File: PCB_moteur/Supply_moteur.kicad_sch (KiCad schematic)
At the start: 63 parts, among them J10 BATT12V, J11 BATT1S, J12 EXT_SW, J9 BATT3S1, Q2 PMOS, Q4 MMBT3904, Q5 IRFR5505TRPBF, SW1 POWER BUTTON, U11 LTC2954ITS8-1, U5 TPS61201DRCR, U8 LM1085-5.0

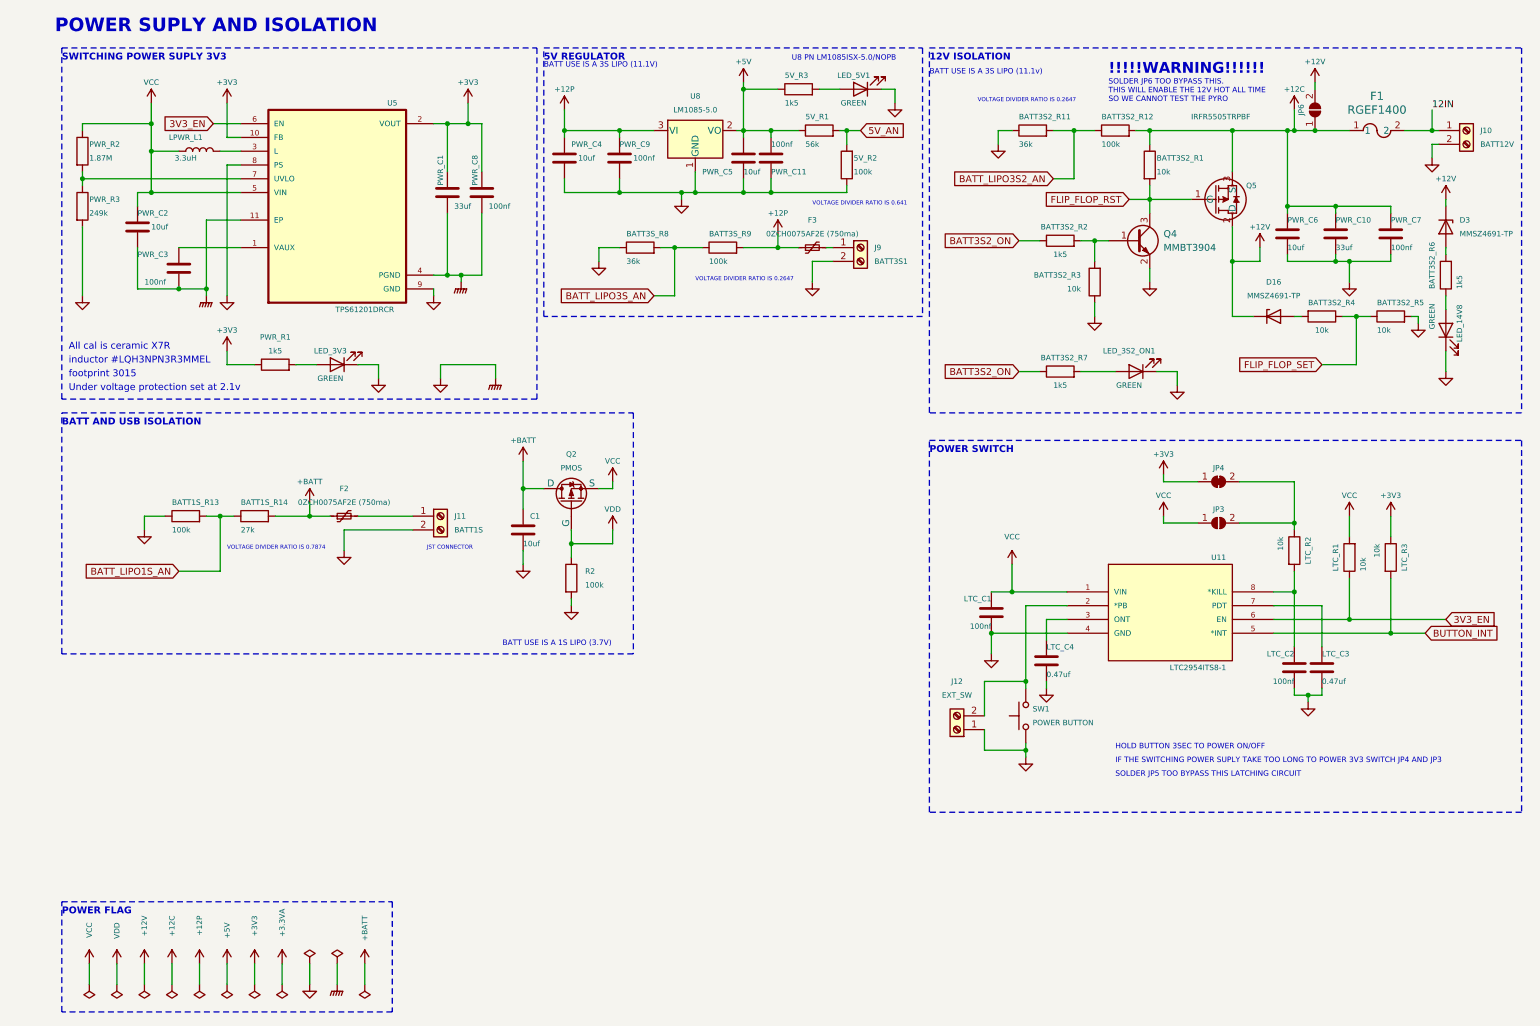
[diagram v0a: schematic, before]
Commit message: Manque supply, pyro et finition (découplage etc)
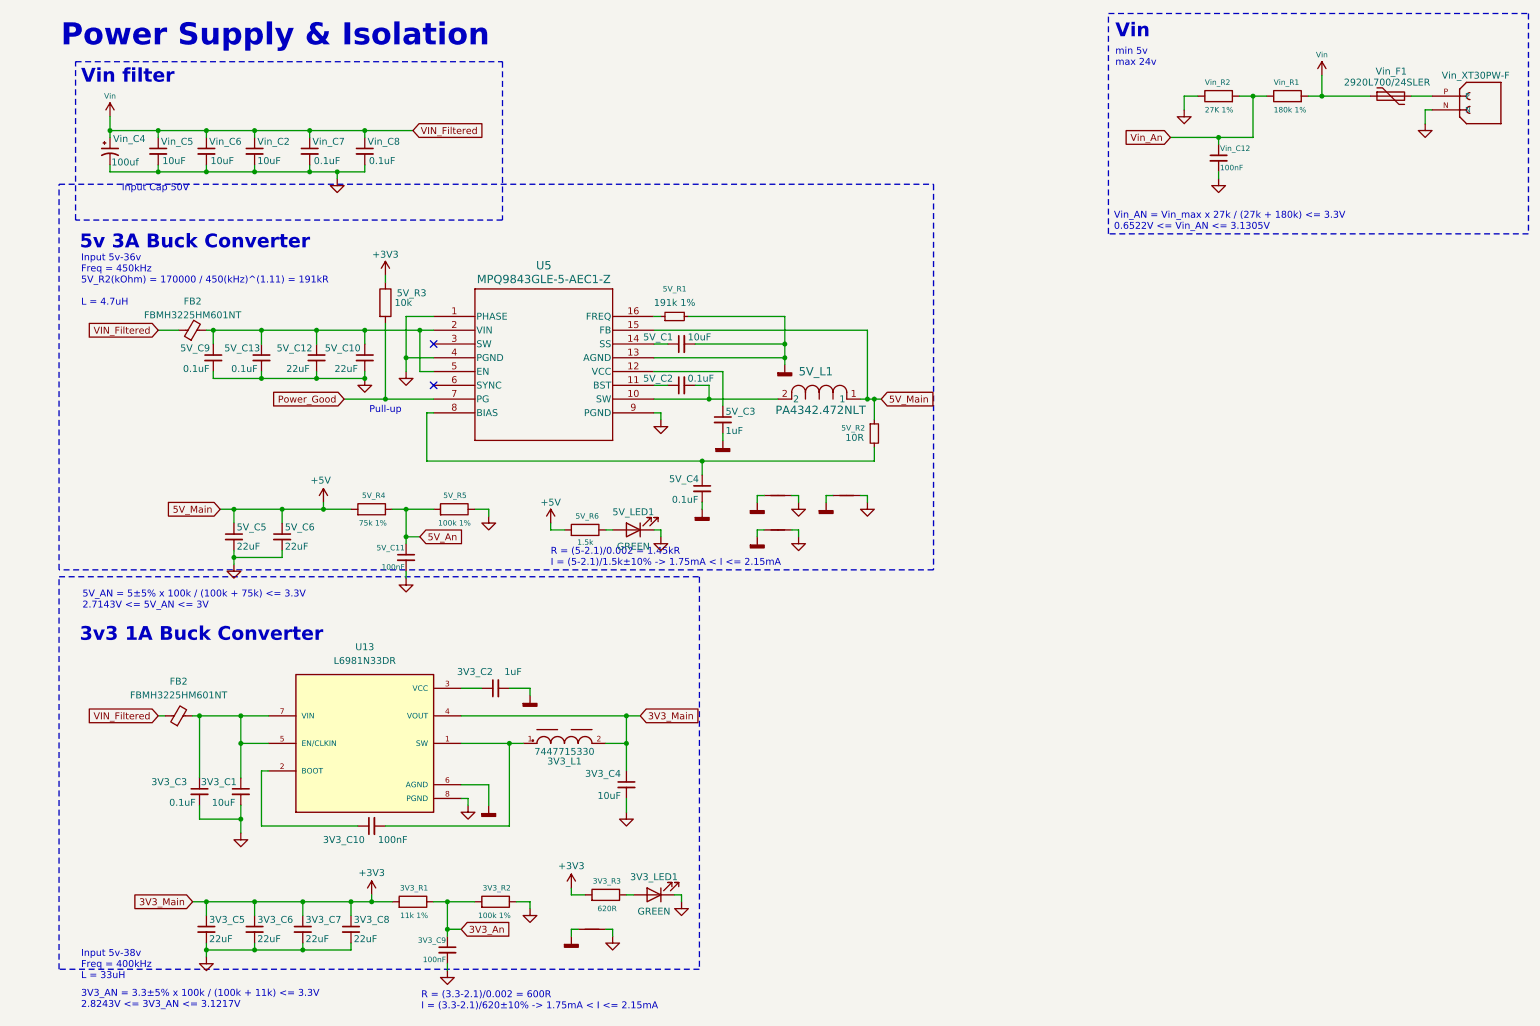
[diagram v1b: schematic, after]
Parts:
- removed 5V_R1: 56k, Resistor_SMD:R_0805_2012Metric, symbol Device:R
- removed 5V_R2, BATT1S_R13, BATT3S2_R12, BATT3S_R9, R2: 100k, Resistor_SMD:R_0805_2012Metric, symbol Device:R
- removed BATT1S_R14: 27k, Resistor_SMD:R_0805_2012Metric, symbol Device:R
- removed BATT3S2_R1, BATT3S2_R3, BATT3S2_R4, BATT3S2_R5, LTC_R1, LTC_R2, LTC_R3: 10k, Resistor_SMD:R_0805_2012Metric, symbol Device:R
- removed BATT3S2_R11, BATT3S_R8: 36k, Resistor_SMD:R_0805_2012Metric, symbol Device:R
- removed BATT3S2_R2, BATT3S2_R6, BATT3S2_R7, PWR_R1: 1k5, Resistor_SMD:R_0805_2012Metric, symbol Device:R
- removed C1, PWR_C2, PWR_C4, PWR_C5: 10uf, Capacitor_SMD:C_0805_2012Metric, symbol Device:C
- removed D16, D3: MMSZ4691-TP, Diode_SMD:D_SOD-123, symbol Diode:BZV55C6V2
- removed F1: RGEF1400, FUS_RGEF1400_TYCO_TYC, symbol RGEF1400:RGEF1400
- removed F2, F3: 0ZCH0075AF2E (750ma), Fuse:Fuse_1210_3225Metric, symbol Device:Polyfuse_Small
- removed J10: BATT12V, Connector_Wire:SolderWire-2.5sqmm_1x02_P8.8mm_D2.4mm_OD4.4mm, symbol Connector:Screw_Terminal_01x02
- removed J11: BATT1S, Connector_JST:JST_XA_B02B-XASK-1_1x02_P2.50mm_Vertical, symbol Connector:Screw_Terminal_01x02
- removed J12: EXT_SW, custom_footprints:B2B-PH-K, symbol Connector:Screw_Terminal_01x02
- removed J9: BATT3S1, Connector_Wire:SolderWire-2.5sqmm_1x02_P8.8mm_D2.4mm_OD4.4mm, symbol Connector:Screw_Terminal_01x02
- removed JP3, JP6: SolderJumper_2_Open, Jumper:SolderJumper-2_P1.3mm_Open_TrianglePad1.0x1.5mm, symbol Jumper:SolderJumper_2_Open
- removed JP4: SolderJumper_2_Bridged, Jumper:SolderJumper-2_P1.3mm_Bridged2Bar_RoundedPad1.0x1.5mm, symbol Jumper:SolderJumper_2_Bridged
- removed LED_14V8, LED_3S2_ON1, LED_3V3, LED_5V1: GREEN, LED_SMD:LED_0805_2012Metric, symbol Device:LED
- removed LPWR_L1: 3.3uH, custom_footprints:IND_LQH3NPN3R3MMEL, symbol Device:L
- removed LTC_C1, LTC_C2, PWR_C11, PWR_C3, PWR_C8, PWR_C9: 100nf, Capacitor_SMD:C_0805_2012Metric, symbol Device:C
- removed LTC_C3, LTC_C4: 0.47uf, Capacitor_SMD:C_0805_2012Metric, symbol Device:C
- removed PWR_C1: 33uf, Capacitor_SMD:C_0805_2012Metric, symbol Device:C
- removed PWR_C10: 33uf, Capacitor_SMD:C_1206_3216Metric, symbol Device:C
- removed PWR_C6: 10uf, Capacitor_SMD:C_1206_3216Metric, symbol Device:C
- removed PWR_C7: 100nf, Capacitor_SMD:C_1206_3216Metric, symbol Device:C
- removed PWR_R2: 1.87M, Resistor_SMD:R_0805_2012Metric, symbol Device:R
- removed PWR_R3: 249k, Resistor_SMD:R_0805_2012Metric, symbol Device:R
- removed Q2: PMOS, Package_TO_SOT_SMD:SOT-23-3, symbol Simulation_SPICE:PMOS
- removed Q4: MMBT3904, Package_TO_SOT_SMD:SOT-23, symbol Transistor_BJT:MMBT3904
- removed Q5: IRFR5505TRPBF, custom_footprints:PG-TO252AA_INF, symbol IRFR5505TRPBF:IRFR5505TRPBF
- removed SW1: POWER BUTTON, Button_Switch_SMD:SW_SPST_Omron_B3FS-105xP, symbol Switch:SW_Omron_B3FS
- removed U11: LTC2954ITS8-1, Package_TO_SOT_SMD:TSOT-23-8, symbol LTC2954ITS8-1_TRPBF:LTC2954ITS8-1#TRPBF
- removed U5: TPS61201DRCR, Package_SON:VSON-10-1EP_3x3mm_P0.5mm_EP1.65x2.4mm, symbol TPS61201DRCR:TPS61201DRCR
- removed U8: LM1085-5.0, Package_TO_SOT_SMD:TO-263-3_TabPin2, symbol Regulator_Linear:LM1085-5.0
- added 3V3_C1, 5V_C1: 10uF, Capacitor_SMD:C_0603_1608Metric, symbol Device:C_Small
- added 3V3_C10, 3V3_C9, 5V_C11, Vin_C12: 100nF, Capacitor_SMD:C_0603_1608Metric, symbol Device:C_Small
- added 3V3_C2, 5V_C3: 1uF, Capacitor_SMD:C_0603_1608Metric, symbol Device:C_Small
- added 3V3_C3, Vin_C7, Vin_C8: 0.1uF, Capacitor_SMD:C_0603_1608Metric, symbol Device:C_Small
- added 3V3_C4, Vin_C2, Vin_C5, Vin_C6: 10uF, Capacitor_SMD:C_1210_3225Metric, symbol Device:C_Small
- added 3V3_C5, 3V3_C6, 3V3_C7, 3V3_C8, 5V_C10, 5V_C12, 5V_C5, 5V_C6: 22uF, Capacitor_SMD:C_1210_3225Metric, symbol Device:C_Small
- added 3V3_L1: 7447715330, ODB:WE-PD_1245, symbol ODB2:WE-PD_1245
- added 3V3_LED1, 5V_LED1: GREEN, LED_SMD:LED_0603_1608Metric, symbol Device:LED
- added 3V3_R1: 11k 1%, Resistor_SMD:R_0603_1608Metric, symbol Device:R
- added 3V3_R2, 5V_R5: 100k 1%, Resistor_SMD:R_0603_1608Metric, symbol Device:R
- added 3V3_R3: 620R, Resistor_SMD:R_0603_1608Metric, symbol Device:R
- added 5V_C13, 5V_C2, 5V_C4, 5V_C9: 0.1uF, Capacitor_SMD:C_0402_1005Metric, symbol Device:C_Small
- added 5V_L1: PA4342.472NLT, ODB:IND_PA4342_PUL, symbol ODB2:PA4342.472NLT
- added 5V_R1: 191k 1%, Resistor_SMD:R_0603_1608Metric, symbol Device:R_Small
- added 5V_R2: 10R, Resistor_SMD:R_0603_1608Metric, symbol Device:R_Small
- added 5V_R4: 75k 1%, Resistor_SMD:R_0603_1608Metric, symbol Device:R
- added 5V_R6: 1.5k, Resistor_SMD:R_0603_1608Metric, symbol Device:R
- added FB2 (x2): FBMH3225HM601NT, Inductor_SMD:L_1210_3225Metric, symbol Device:FerriteBead_Small
- added J15: Vin_XT30PW-F, ODB:AMASS_XT30PW-F, symbol ODB2:XT30PW-F
- added NT1, NT2, NT5: NetTie_2, NetTie:NetTie-2_SMD_Pad0.5mm, symbol Device:NetTie_2
- added NT4: NetTie_2, NetTie:NetTie-4_SMD_Pad0.5mm, symbol Device:NetTie_2
- added U13: L6981N33DR, ODB:SOIC127P600X175-8N, symbol ODB2:L6981N33DR
- added U5: MPQ9843GLE-5-AEC1-Z, ODB:QFN-16_ MPQ9843, symbol ODB2:MPQ9843GLE-5-AEC1-Z
- added Vin_C4: 100uf, ODB:WCAP-PSHP_8X8.7_DXL_, symbol ODB2:875115652007
- added Vin_F1: 2920L700/24SLER, Fuse:Fuse_2920_7451Metric, symbol Device:Polyfuse
- added Vin_R1: 180k 1%, Resistor_SMD:R_0603_1608Metric, symbol Device:R
- added Vin_R2: 27K 1%, Resistor_SMD:R_0603_1608Metric, symbol Device:R
- 5V_R3: value 1k5 -> 10k; footprint Resistor_SMD:R_0805_2012Metric -> Resistor_SMD:R_0603_1608Metric
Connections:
- net +3V3: now also 5V_R3.1, 3V3_C4.1, 3V3_C5.1, 3V3_C6.1, 3V3_C7.1, 3V3_C8.1, 3V3_L1.2, 3V3_R1.2, 3V3_R3.2, U13.4 (VOUT)
- net +5V: now also 5V_C5.1, 5V_C6.1, 5V_L1.1, 5V_R2.1, 5V_R4.2, 5V_R6.2, U5.15 (FB); no longer 5V_R3.1
- net GND: now also 3V3_C1.2, 3V3_C3.2, 3V3_C4.2, 3V3_C5.2, 3V3_C6.2, 3V3_C7.2, 3V3_C8.2, 3V3_C9.2, 3V3_LED1.1 (K), 3V3_R2.1, 5V_C10.2, 5V_C11.2, 5V_C12.2, 5V_C13.2, 5V_C5.2, 5V_C6.2, 5V_C9.2, 5V_LED1.1 (K), 5V_R5.1, J15.N, NT1.2, NT2.2, NT4.2, NT5.2, U13.8 (PGND), U5.1 (PHASE), U5.4 (PGND), U5.9 (PGND), Vin_C12.2, Vin_C2.2, Vin_C4.2, Vin_C5.2, Vin_C6.2, Vin_C7.2, Vin_C8.2, Vin_R2.1
- net Power_Good: now reaches 5V_R3.2
- net Power_Good: now also U5.7 (PG)
- new net: 5V_LED1.2 (A), 5V_R6.1
- new net: 5V_C2.2, 5V_L1.2, U5.10 (SW)
- new net: 5V_R1.1, U5.16 (FREQ)
- new net: 3V3_C1.1, 3V3_C3.1, FB2.2, U13.5 (EN/CLKIN), U13.7 (VIN)
- new net: 3V3_C2.1, U13.3 (VCC)
- new net: 3V3_C10.2, 3V3_L1.1, U13.1 (SW)
- new net: 5V_C10.1, 5V_C12.1, 5V_C13.1, 5V_C9.1, FB2.2, U5.2 (VIN), U5.5 (EN)
- new net: 3V3_LED1.2 (A), 3V3_R3.1
- new net: 5V_C4.1, 5V_R2.2, U5.8 (BIAS)
- new net: J15.P, Vin_F1.2
- new net: 3V3_C10.1, U13.2 (BOOT)
- new net: 5V_C2.1, U5.11 (BST)
- new net: 5V_C1.1, U5.14 (SS)
- new net: 5V_C3.1, U5.12 (VCC)
- new net 3V3_An: 3V3_C9.1, 3V3_R1.1, 3V3_R2.2
- new net 5V_An: 5V_C11.1, 5V_R4.1, 5V_R5.2
- new net AGND3V3: 3V3_C2.2, NT4.1, U13.6 (AGND)
- new net AGND5V: 5V_C1.2, 5V_C3.2, 5V_C4.2, 5V_R1.2, NT1.1, NT2.1, NT5.1, U5.13 (AGND)
- new net Vin: FB2.1, FB2.1, Vin_C2.1, Vin_C4.1, Vin_C5.1, Vin_C6.1, Vin_C7.1, Vin_C8.1, Vin_F1.1, Vin_R1.2
- new net Vin_An: Vin_C12.1, Vin_R1.1, Vin_R2.2
- no-connect marks 0 -> 2
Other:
- note added: "3V3_AN = 3.3±5% x 100k / (100k + 11k) <= 3.3V 2.8243V <= 3V3_AN <= 3.1217V"
- note added: "3v3 1A Buck Converter"
- note added: "5V_AN = 5±5% x 100k / (100k + 75k) <= 3.3V 2.7143V <= 5V_AN <= 3V"
- note added: "5v 3A Buck Converter"
- note added: "Input 5v-36v Freq = 450kHz 5V_R2(kOhm) = 170000 / 450(kHz)^(1.11) = 191kR L = 4.7uH"
- note added: "Input 5v-38v Freq = 400kHz L = 33uH"
- note added: "Input Cap 50V"
- note added: "Power Supply & Isolation"
- note added: "Pull-up"
- note added: "R = (3.3-2.1)/0.002 = 600R I = (3.3-2.1)/620±10% -> 1.75mA < I <= 2.15mA"
- note added: "R = (5-2.1)/0.002 = 1.45kR I = (5-2.1)/1.5k±10% -> 1.75mA < I <= 2.15mA"
- note added: "Vin"
- note added: "Vin filter"
- note added: "Vin_AN = Vin_max x 27k / (27k + 180k) <= 3.3V 0.6522V <= Vin_AN <= 3.1305V"
- note added: "min 5v max 24v"
- note removed: "!!!!!WARNING!!!!!!"
- note removed: "12V ISOLATION"
- note removed: "5V REGULATOR"
- note removed: "All cal is ceramic X7R"
- note removed: "BATT AND USB ISOLATION"
- note removed: "BATT USE IS A 1S LIPO (3.7V)"
- note removed: "BATT USE IS A 3S LIPO (11.1V)"
- note removed: "BATT USE IS A 3S LIPO (11.1v)"
- note removed: "HOLD BUTTON 3SEC TO POWER ON/OFF"
- note removed: "IF THE SWITCHING POWER SUPLY TAKE TOO LONG TO POWER 3V3 SWITCH JP4 AND JP3"
- note removed: "JST CONNECTOR"
- note removed: "POWER FLAG"
- note removed: "POWER SUPLY AND ISOLATION"
- note removed: "POWER SWITCH"
- note removed: "SOLDER JP5 TOO BYPASS THIS LATCHING CIRCUIT"
- note removed: "SOLDER JP6 TOO BYPASS THIS. THIS WILL ENABLE THE 12V HOT ALL TIME SO WE CANNOT TEST THE PYRO"
- note removed: "SWITCHING POWER SUPLY 3V3"
- note removed: "U8 PN LM1085ISX-5.0/NOPB"
- note removed: "Under voltage protection set at 2.1v"
- note removed: "VOLTAGE DIVIDER RATIO IS 0.2647"
- note removed: "VOLTAGE DIVIDER RATIO IS 0.641"
- note removed: "VOLTAGE DIVIDER RATIO IS 0.7874"
- note removed: "footprint 3015"
- note removed: "inductor #LQH3NPN3R3MMEL"

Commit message: wip: remove unnecessary components
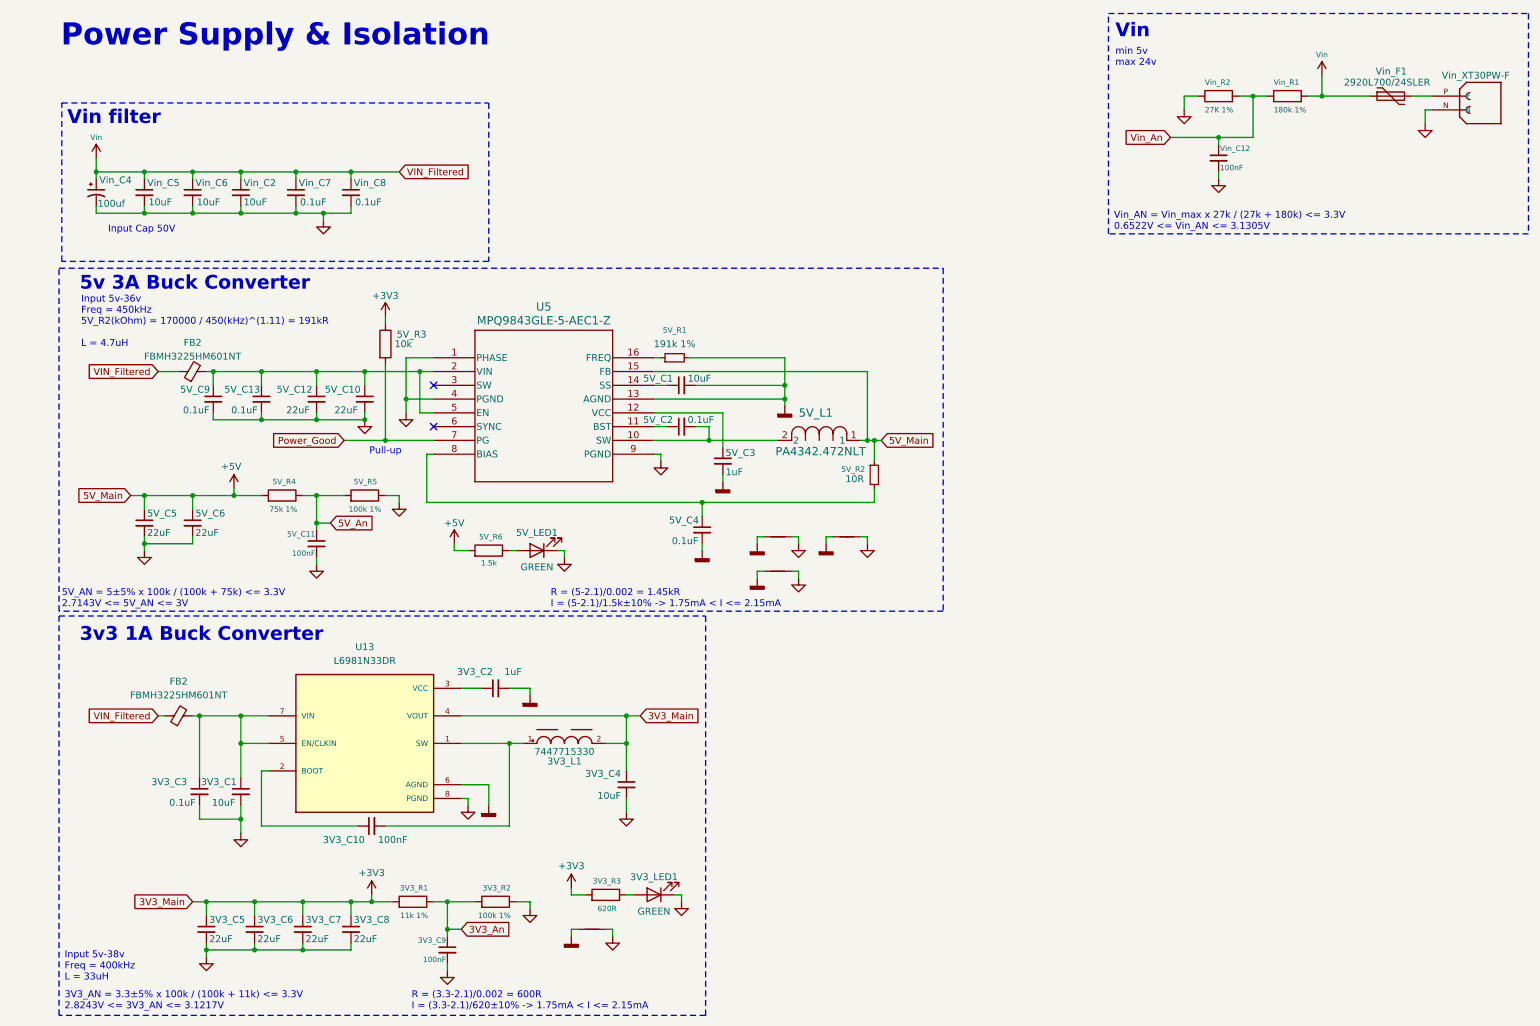
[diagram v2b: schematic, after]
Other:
- moved on the sheet: 5V_C1, 5V_C10, 5V_C11, 5V_C12, 5V_C13, 5V_C2, 5V_C3, 5V_C4, 5V_C5, 5V_C6, 5V_C9, 5V_L1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

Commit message: fix: power supply + add LED RG + add mounting holes + change 6pins header SWD connector + pyros
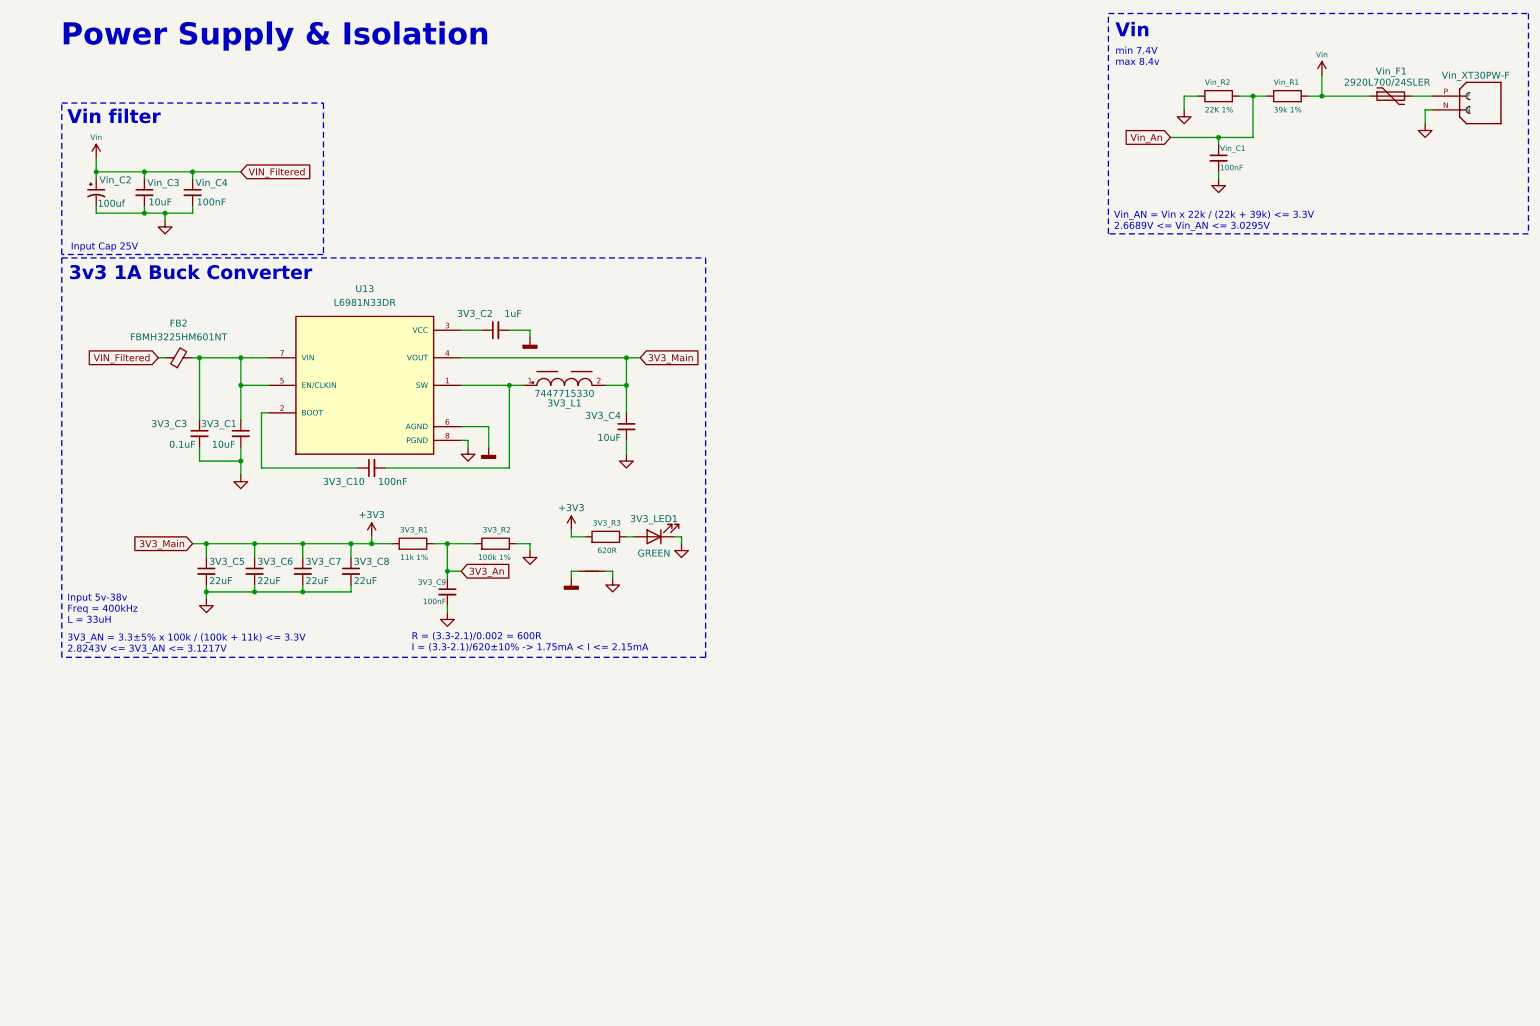
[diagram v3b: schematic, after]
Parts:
- removed 5V_C1: 10uF, Capacitor_SMD:C_0603_1608Metric, symbol Device:C_Small
- removed 5V_C10, 5V_C12, 5V_C5, 5V_C6: 22uF, Capacitor_SMD:C_1210_3225Metric, symbol Device:C_Small
- removed 5V_C11: 100nF, Capacitor_SMD:C_0603_1608Metric, symbol Device:C_Small
- removed 5V_C13, 5V_C2, 5V_C4, 5V_C9: 0.1uF, Capacitor_SMD:C_0402_1005Metric, symbol Device:C_Small
- removed 5V_C3: 1uF, Capacitor_SMD:C_0603_1608Metric, symbol Device:C_Small
- removed 5V_L1: PA4342.472NLT, ODB:IND_PA4342_PUL, symbol ODB2:PA4342.472NLT
- removed 5V_LED1: GREEN, LED_SMD:LED_0603_1608Metric, symbol Device:LED
- removed 5V_R1: 191k 1%, Resistor_SMD:R_0603_1608Metric, symbol Device:R_Small
- removed 5V_R2: 10R, Resistor_SMD:R_0603_1608Metric, symbol Device:R_Small
- removed 5V_R3: 10k, Resistor_SMD:R_0603_1608Metric, symbol Device:R
- removed 5V_R4: 75k 1%, Resistor_SMD:R_0603_1608Metric, symbol Device:R
- removed 5V_R5: 100k 1%, Resistor_SMD:R_0603_1608Metric, symbol Device:R
- removed 5V_R6: 1.5k, Resistor_SMD:R_0603_1608Metric, symbol Device:R
- removed FB2: FBMH3225HM601NT, Inductor_SMD:L_1210_3225Metric, symbol Device:FerriteBead_Small
- removed NT1, NT2, NT5: NetTie_2, NetTie:NetTie-2_SMD_Pad0.5mm, symbol Device:NetTie_2
- removed U5: MPQ9843GLE-5-AEC1-Z, ODB:QFN-16_ MPQ9843, symbol ODB2:MPQ9843GLE-5-AEC1-Z
- removed Vin_C2, Vin_C6: 10uF, Capacitor_SMD:C_1210_3225Metric, symbol Device:C_Small
- removed Vin_C7: 0.1uF, Capacitor_SMD:C_0603_1608Metric, symbol Device:C_Small
- Vin_C4: renamed from Vin_C8; value 0.1uF -> 100nF
- Vin_R1: value 180k 1% -> 39k 1%
- Vin_R2: value 27K 1% -> 22K 1%
- renumbered Vin_C12 to Vin_C1, Vin_C4 to Vin_C2, Vin_C5 to Vin_C3
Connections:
- no-connect marks 2 -> 0
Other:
- note added: "Input Cap 25V"
- note added: "Vin_AN = Vin x 22k / (22k + 39k) <= 3.3V 2.6689V <= Vin_AN <= 3.0295V"
- note added: "min 7.4V max 8.4v"
- note removed: "5V_AN = 5±5% x 100k / (100k + 75k) <= 3.3V 2.7143V <= 5V_AN <= 3V"
- note removed: "5v 3A Buck Converter"
- note removed: "Input 5v-36v Freq = 450kHz 5V_R2(kOhm) = 170000 / 450(kHz)^(1.11) = 191kR L = 4.7uH"
- note removed: "Input Cap 50V"
- note removed: "Pull-up"
- note removed: "R = (5-2.1)/0.002 = 1.45kR I = (5-2.1)/1.5k±10% -> 1.75mA < I <= 2.15mA"
- note removed: "Vin_AN = Vin_max x 27k / (27k + 180k) <= 3.3V 0.6522V <= Vin_AN <= 3.1305V"
- note removed: "min 5v max 24v"
- moved on the sheet: 3V3_C1, 3V3_C10, 3V3_C2, 3V3_C3, 3V3_C4, 3V3_C5, 3V3_C6, 3V3_C7, 3V3_C8, 3V3_C9, 3V3_L1, 3V3_LED1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
